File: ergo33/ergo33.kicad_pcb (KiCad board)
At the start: 2 copper layers, 173.8 x 117.1 mm, 124 parts, among them SW1 SW_Push, SW46 Rotary_Encoder_Switch, U1 ATmega32U4-AU, U2 USBLC6-2SC6, Y1 16MHz

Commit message: ergo33: fix a derp
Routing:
- net +5V: track 488.0 -> 494.9 mm, vias 11 -> 10
- net GND: track 174.1 -> 175.4 mm
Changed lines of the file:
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@@
     (thickness 1.6)
     (drawings 18)
-    (tracks 954)
+    (tracks 952)
     (zones 0)
     (modules 124)
@@
     (47 F.CrtYd user)
     (48 B.Fab user)
-    (49 F.Fab user)
+    (49 F.Fab user hide)
   )
   (setup
@@
   (segment (start 180.8 34.5375) (end 182.9625 34.5375) (width 0.375) (layer B.Cu) (net 2))
   (segment (start 182.9625 34.5375) (end 183 34.5) (width 0.375) (layer B.Cu) (net 2))
-  (segment (start 170.029999 34.895) (end 170.005 34.895) (width 0.375) (layer B.Cu) (net 2))
-  (via (at 168.1 36.8) (size 0.8) (drill 0.4) (layers F.Cu B.Cu) (net 2))
-  (segment (start 170.005 34.895) (end 168.1 36.8) (width 0.375) (layer B.Cu) (net 2))
-  (via (at 178.3 36.8) (size 0.8) (drill 0.4) (layers F.Cu B.Cu) (net 2))
-  (segment (start 176.479999 34.895) (end 176.479999 34.979999) (width 0.375) (layer B.Cu) (net 2))
-  (segment (start 176.479999 34.979999) (end 178.3 36.8) (width 0.375) (layer B.Cu) (net 2))
   (via (at 173.6 47.2) (size 0.8) (drill 0.4) (layers F.Cu B.Cu) (net 2))
   (segment (start 173.6 45.2375) (end 173.6 47.2) (width 0.375) (layer B.Cu) (net 2))
@@
   (segment (start 191.3 68.4) (end 189.5 70.2) (width 0.375) (layer B.Cu) (net 2))
   (via (at 191.3 68.4) (size 0.8) (drill 0.4) (layers F.Cu B.Cu) (net 2))
+  (via (at 178.2 37.6) (size 0.8) (drill 0.4) (layers F.Cu B.Cu) (net 2))
+  (segment (start 176.479999 34.895) (end 176.479999 35.879999) (width 0.375) (layer B.Cu) (net 2))
+  (segment (start 176.479999 35.879999) (end 178.2 37.6) (width 0.375) (layer B.Cu) (net 2))
+  (via (at 168.4 37.5) (size 0.8) (drill 0.4) (layers F.Cu B.Cu) (net 2))
+  (segment (start 170.029999 34.895) (end 170.029999 35.870001) (width 0.375) (layer B.Cu) (net 2))
+  (segment (start 170.029999 35.870001) (end 168.4 37.5) (width 0.375) (layer B.Cu) (net 2))
   (segment (start 173.4625 43.4) (end 173.6 43.5375) (width 0.375) (layer B.Cu) (net 87))
   (segment (start 187.770953 64.140912) (end 187.275978 63.645937) (width 0.25) (layer B.Cu) (net 3))
@@
   (segment (start 178.1625 54.1625) (end 178.1625 53.9625) (width 0.375) (layer B.Cu) (net 4))
   (segment (start 178.1625 56.1) (end 178.1625 54.1625) (width 0.375) (layer B.Cu) (net 4))
-  (segment (start 188.9 46.4) (end 190.5 48) (width 0.375) (layer F.Cu) (net 4))
-  (segment (start 179.8 46.4) (end 188.9 46.4) (width 0.375) (layer F.Cu) (net 4))
-  (segment (start 177.3425 78.7) (end 175.1425 80.9) (width 0.375) (layer F.Cu) (net 4))
-  (segment (start 186.4 78.7) (end 177.3425 78.7) (width 0.375) (layer F.Cu) (net 4))
   (segment (start 175.1425 80.9) (end 173.8 80.9) (width 0.375) (layer F.Cu) (net 4))
   (segment (start 166.1 88.6) (end 165.1 88.6) (width 0.375) (layer F.Cu) (net 4))
@@
   (segment (start 164.6 88.6) (end 165.1 88.6) (width 0.375) (layer F.Cu) (net 4))
   (segment (start 165.1 88.6) (end 165.6 88.6) (width 0.375) (layer F.Cu) (net 4))
-  (segment (start 186.4 78.7) (end 187.6 78.7) (width 0.25) (layer F.Cu) (net 4))
-  (segment (start 187.6 78.7) (end 192.7 73.6) (width 0.25) (layer F.Cu) (net 4))
-  (via (at 190.8 56.3) (size 0.8) (drill 0.4) (layers F.Cu B.Cu) (net 4))
-  (segment (start 192.7 73.6) (end 192.7 58.2) (width 0.25) (layer F.Cu) (net 4))
-  (segment (start 192.7 58.2) (end 190.8 56.3) (width 0.25) (layer F.Cu) (net 4))
   (segment (start 187.675 56.3) (end 187.6 56.225) (width 0.25) (layer B.Cu) (net 4))
-  (segment (start 190.8 56.3) (end 187.675 56.3) (width 0.25) (layer B.Cu) (net 4))
+  (segment (start 189.8 46.4) (end 179.8 46.4) (width 0.375) (layer F.Cu) (net 4))
+  (segment (start 191.1 47.7) (end 189.8 46.4) (width 0.375) (layer F.Cu) (net 4))
+  (segment (start 177.3425 78.7) (end 188.6 78.7) (width 0.375) (layer F.Cu) (net 4))
+  (segment (start 175.1425 80.9) (end 177.3425 78.7) (width 0.375) (layer F.Cu) (net 4))
+  (segment (start 188.6 78.7) (end 193.3 74) (width 0.375) (layer F.Cu) (net 4))
+  (segment (start 193.3 60.1) (end 191.1 57.9) (width 0.375) (layer F.Cu) (net 4))
+  (segment (start 191.1 57.9) (end 191.1 47.7) (width 0.375) (layer F.Cu) (net 4))
+  (segment (start 193.3 74) (end 193.3 60.1) (width 0.375) (layer F.Cu) (net 4))
   (segment (start 174.9125 58.225) (end 175.4 57.7375) (width 0.375) (layer B.Cu) (net 5))
   (segment (start 174.9125 60.51125) (end 174.9125 58.225) (width 0.375) (layer B.Cu) (net 5))

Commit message: Add external light PCB
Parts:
- added CExt1: 0,1uF, Capacitor_SMD:C_0805_2012Metric_Pad1.15x1.40mm_HandSolder, F.Cu at (36.9, 120.9)
- added CExt2: 0,1uF, Capacitor_SMD:C_0805_2012Metric_Pad1.15x1.40mm_HandSolder, F.Cu at (45.8, 120.8)
- added CExt3: 0,1uF, Capacitor_SMD:C_0805_2012Metric_Pad1.15x1.40mm_HandSolder, F.Cu at (54.7, 120.8)
- added CExt4: 0,1uF, Capacitor_SMD:C_0805_2012Metric_Pad1.15x1.40mm_HandSolder, F.Cu at (63.6, 120.8)
- added JExt1: Conn_01x03, Connector_PinHeader_2.54mm:PinHeader_1x03_P2.54mm_Vertical, B.Cu at (27.1, 126.8)
- added LEDExt1: WS2812B, LED_SMD:LED_WS2812B_PLCC4_5.0x5.0mm_P3.2mm, F.Cu at (38.3, 125.0)
- added LEDExt2: WS2812B, LED_SMD:LED_WS2812B_PLCC4_5.0x5.0mm_P3.2mm, F.Cu at (47.2, 125.0)
- added LEDExt3: WS2812B, LED_SMD:LED_WS2812B_PLCC4_5.0x5.0mm_P3.2mm, F.Cu at (56.1, 125.0)
- added LEDExt4: WS2812B, LED_SMD:LED_WS2812B_PLCC4_5.0x5.0mm_P3.2mm, F.Cu at (65.0, 125.0)
- added REF**: MountingHole_2.2mm_M2_ISO7380_Pad_Courtyard, tunks-parts:MountingHole_2.2mm_M2_ISO7380_Pad_Courtyard, F.Cu at (27.1, 120.8)
- added REF**: MountingHole_2.2mm_M2_ISO7380_Pad_Courtyard, tunks-parts:MountingHole_2.2mm_M2_ISO7380_Pad_Courtyard, F.Cu at (27.1, 137.9)
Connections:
- JLED1 pad 1: +5V -> GND
- JLED1 pad 3: GND -> +5V
- U1 pad 1: Net-(U1-Pad1) -> (no net)
- U1 pad 10: Net-(U1-Pad10) -> (no net)
- U1 pad 11: Net-(U1-Pad11) -> (no net)
- U1 pad 12: Net-(U1-Pad12) -> (no net)
- U1 pad 18: Net-(U1-Pad18) -> (no net)
- U1 pad 19: Net-(U1-Pad19) -> (no net)
- U1 pad 20: Net-(U1-Pad20) -> (no net)
- U1 pad 26: Net-(U1-Pad26) -> (no net)
- U1 pad 42: Net-(U1-Pad42) -> (no net)
- U1 pad 8: Net-(U1-Pad8) -> (no net)
- U1 pad 9: Net-(U1-Pad9) -> (no net)
- USB1 pad 3: Net-(USB1-Pad3) -> (no net)
- USB1 pad 9: Net-(USB1-Pad9) -> (no net)
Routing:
- net 5VExt: track 0.00 -> 73.8 mm
- net Net-(JExt1-Pad2): track 0.00 -> 9.91 mm
- net Net-(LEDExt2-Pad2): track 0.00 -> 5.33 mm
- net Net-(LEDExt3-Pad2): track 0.00 -> 5.33 mm
- net Net-(LEDExt1-Pad2): track 0.00 -> 5.32 mm
- net LEDS2: track 19.4 -> 18.1 mm
- net GND: track 175.4 -> 176.4 mm
- net +5V: track 494.9 -> 494.1 mm
- added copper zone on F.Cu, net GNDExt
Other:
- board size 173.8 x 117.1 mm -> 173.8 x 122.5 mm
- board text added: "Layer"
- board text added: "Mode"

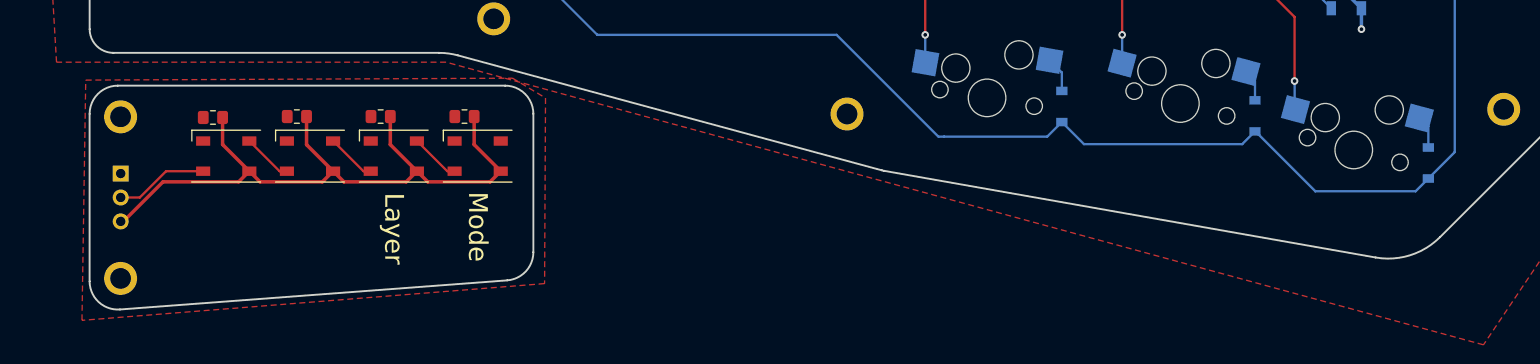
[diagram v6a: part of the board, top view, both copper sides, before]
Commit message: ergo33: minor cleanup
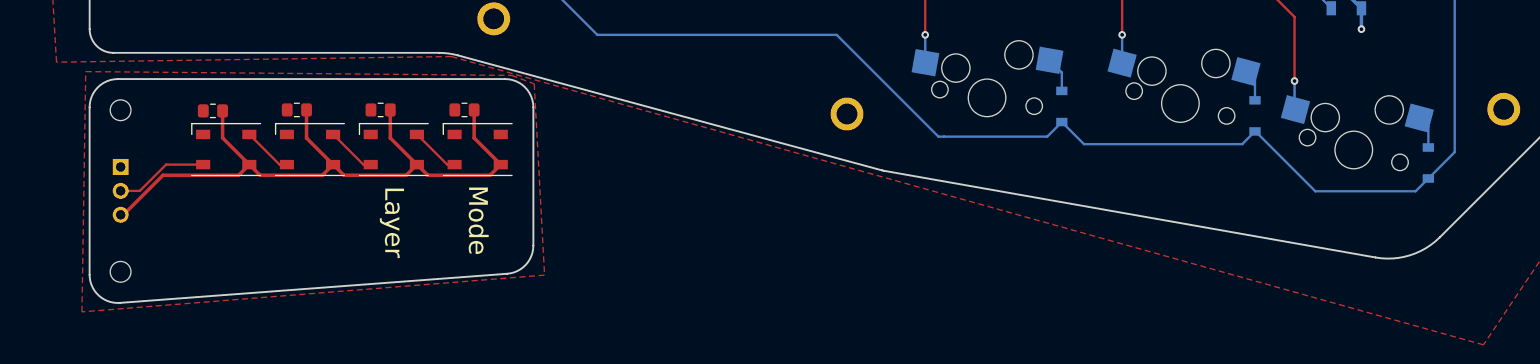
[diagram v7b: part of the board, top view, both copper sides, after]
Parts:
- removed the REF** at (27.1, 120.8)
- removed the REF** at (27.1, 137.9)
- added M1: MountingHole_2.2mm_M2_ISO7380, MountingHole:MountingHole_2.2mm_M2_ISO7380, F.Cu at (27.1, 120.1)
- added M2: MountingHole_2.2mm_M2_ISO7380, MountingHole:MountingHole_2.2mm_M2_ISO7380, F.Cu at (27.1, 137.2)
- moved CExt1 0.70 mm to (36.9, 120.2)
- moved CExt2 0.70 mm to (45.8, 120.1)
- moved CExt3 0.70 mm to (54.7, 120.1)
- moved CExt4 0.70 mm to (63.6, 120.1)
- moved LEDExt1 0.70 mm to (38.3, 124.3)
- moved LEDExt2 0.70 mm to (47.2, 124.3)
- moved LEDExt3 0.70 mm to (56.1, 124.3)
- moved LEDExt4 0.70 mm to (65.0, 124.3)
- moved JExt1 0.70 mm to (27.1, 126.1)
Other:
- board size 173.8 x 122.5 mm -> 173.8 x 121.8 mm

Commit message: ergo33: minor tweaking
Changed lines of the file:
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@@
     (polygon
       (pts
-        (xy 196.8 27.4) (xy 201 101.5) (xy 171.75 145) (xy 62.2 114.4) (xy 20.3 115)
+        (xy 196.8 27.4) (xy 201 101.5) (xy 171.8 144.1) (xy 62.4 114.3) (xy 20.3 115)
         (xy 14.7 20) (xy 23.2 16.5) (xy 82.2 16.5)
       )
@@
     (polygon
       (pts
-        (xy 68.6 116.4) (xy 71 117.3) (xy 72.1 137.6) (xy 23 141.5) (xy 23.4 116)
+        (xy 68.4 116.6) (xy 70.9 117.7) (xy 72.1 137.6) (xy 23 141.5) (xy 23.4 116)
       )
     )
